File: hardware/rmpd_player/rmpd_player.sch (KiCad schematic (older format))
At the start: 37 parts

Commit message: spi stub
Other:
- moved on the sheet: C?, R?
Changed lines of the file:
@@
 L Device:R R?
 U 1 1 5C090195
-P 4400 1100
-F 0 "R?" H 4200 1150 50  0000 L CNN
-F 1 "10k" H 4200 1050 50  0000 L CNN
-F 2 "" V 4330 1100 50  0001 C CNN
-F 3 "~" H 4400 1100 50  0001 C CNN
-	1    4400 1100
-	1    0    0    -1
-$EndComp
-$Comp
-L Device:C C?
-U 1 1 5C0902B0
 P 4400 1500
-F 0 "C?" H 4550 1450 50  0000 C CNN
-F 1 "100n" H 4600 1550 50  0000 C CNN
-F 2 "" H 4438 1350 50  0001 C CNN
+F 0 "R?" H 4200 1550 50  0000 L CNN
+F 1 "10k" H 4200 1450 50  0000 L CNN
+F 2 "" V 4330 1500 50  0001 C CNN
 F 3 "~" H 4400 1500 50  0001 C CNN
 	1    4400 1500
-	-1   0    0    1
-$EndComp
-Text GLabel 4400 1700 3    50   Input ~ 0
+	1    0    0    -1
+$EndComp
+$Comp
+L Device:C C?
+U 1 1 5C0902B0
+P 4400 1900
+F 0 "C?" H 4550 1850 50  0000 C CNN
+F 1 "100n" H 4600 1950 50  0000 C CNN
+F 2 "" H 4438 1750 50  0001 C CNN
+F 3 "~" H 4400 1900 50  0001 C CNN
+	1    4400 1900
+	-1   0    0    1
+$EndComp
+Text GLabel 4400 2100 3    50   Input ~ 0
 GND
-Text GLabel 4400 900  1    50   Input ~ 0
+Text GLabel 4400 1300 1    50   Input ~ 0
 VDD
 Wire Wire Line
-	4400 900  4400 950
-Wire Wire Line
-	4400 1700 4400 1650
-Wire Wire Line
-	4400 1250 4400 1300
-Wire Wire Line
-	4400 1300 4650 1300
-Wire Wire Line
-	4650 1300 4650 1700
-Wire Wire Line
-	4650 1700 5050 1700
-Connection ~ 4400 1300
-Wire Wire Line
 	4400 1300 4400 1350
+Wire Wire Line
+	4400 2100 4400 2050
+Wire Wire Line
+	4400 1650 4400 1700
+Connection ~ 4400 1700
+Wire Wire Line
+	4400 1700 4400 1750
 Wire Wire Line
 	6900 2650 7250 2650
@@
 Wire Wire Line
 	6950 2350 6900 2350
-Text GLabel 2550 5750 0    50   Input ~ 0
+Text GLabel 2600 5750 0    50   Input ~ 0
 VDDA
-Text GLabel 3100 5750 2    50   Input ~ 0
+Text GLabel 3050 5750 2    50   Input ~ 0
 VDD
 $Comp
@@
 $EndComp
 Wire Wire Line
-	2550 5750 2700 5750
+	2600 5750 2700 5750
 Wire Wire Line
 	2950 5800 2950 5750
 Connection ~ 2950 5750
 Wire Wire Line
-	2950 5750 3100 5750
+	2950 5750 3050 5750
 Wire Wire Line
 	2700 5800 2700 5750
@@
 Wire Wire Line
 	2700 5750 2950 5750
-$Comp
-L power:GND #PWR?
-U 1 1 5C092AF6
-P 2950 6200
-F 0 "#PWR?" H 2950 5950 50  0001 C CNN
-F 1 "GND" H 2955 6027 50  0000 C CNN
-F 2 "" H 2950 6200 50  0001 C CNN
-F 3 "" H 2950 6200 50  0001 C CNN
-	1    2950 6200
-	1    0    0    -1
-$EndComp
-$Comp
-L power:GNDA #PWR?
-U 1 1 5C092B4B
-P 2700 6200
-F 0 "#PWR?" H 2700 5950 50  0001 C CNN
-F 1 "GNDA" H 2705 6027 50  0000 C CNN
-F 2 "" H 2700 6200 50  0001 C CNN
-F 3 "" H 2700 6200 50  0001 C CNN
-	1    2700 6200
-	1    0    0    -1
-$EndComp
-Wire Wire Line
-	2950 6100 2950 6200
-Wire Wire Line
-	2700 6100 2700 6200
+Wire Wire Line
+	2950 6100 2950 6150
+Wire Wire Line
+	2700 6100 2700 6150
+Wire Wire Line
+	4400 1700 5050 1700
+Text GLabel 2950 6150 3    50   Input ~ 0
+GND
+Text GLabel 2700 6150 3    50   Input ~ 0
+GNDA
 $EndSCHEMATC

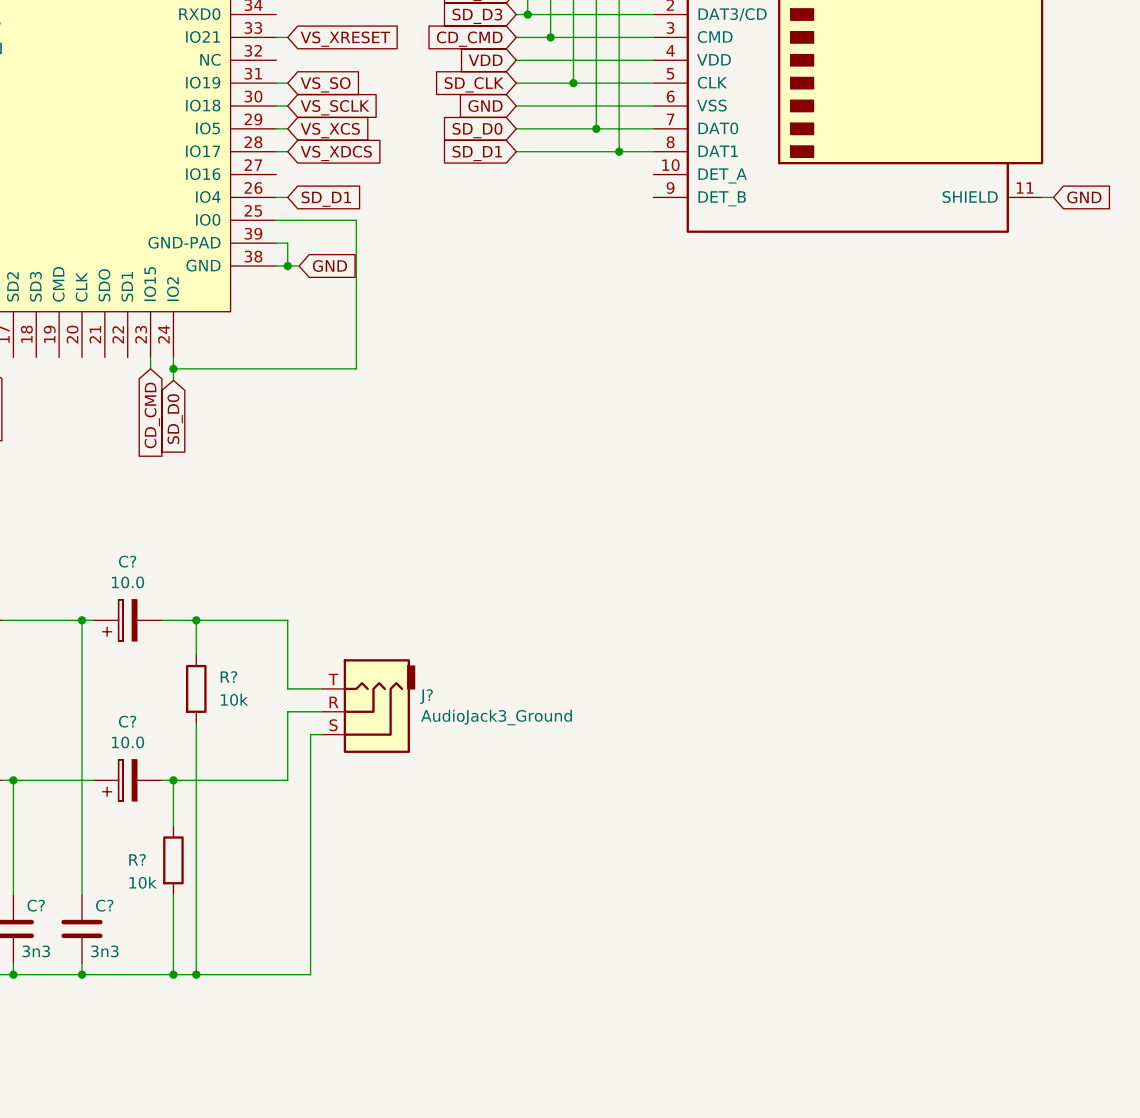
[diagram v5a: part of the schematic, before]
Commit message: vs1011 mute circuit
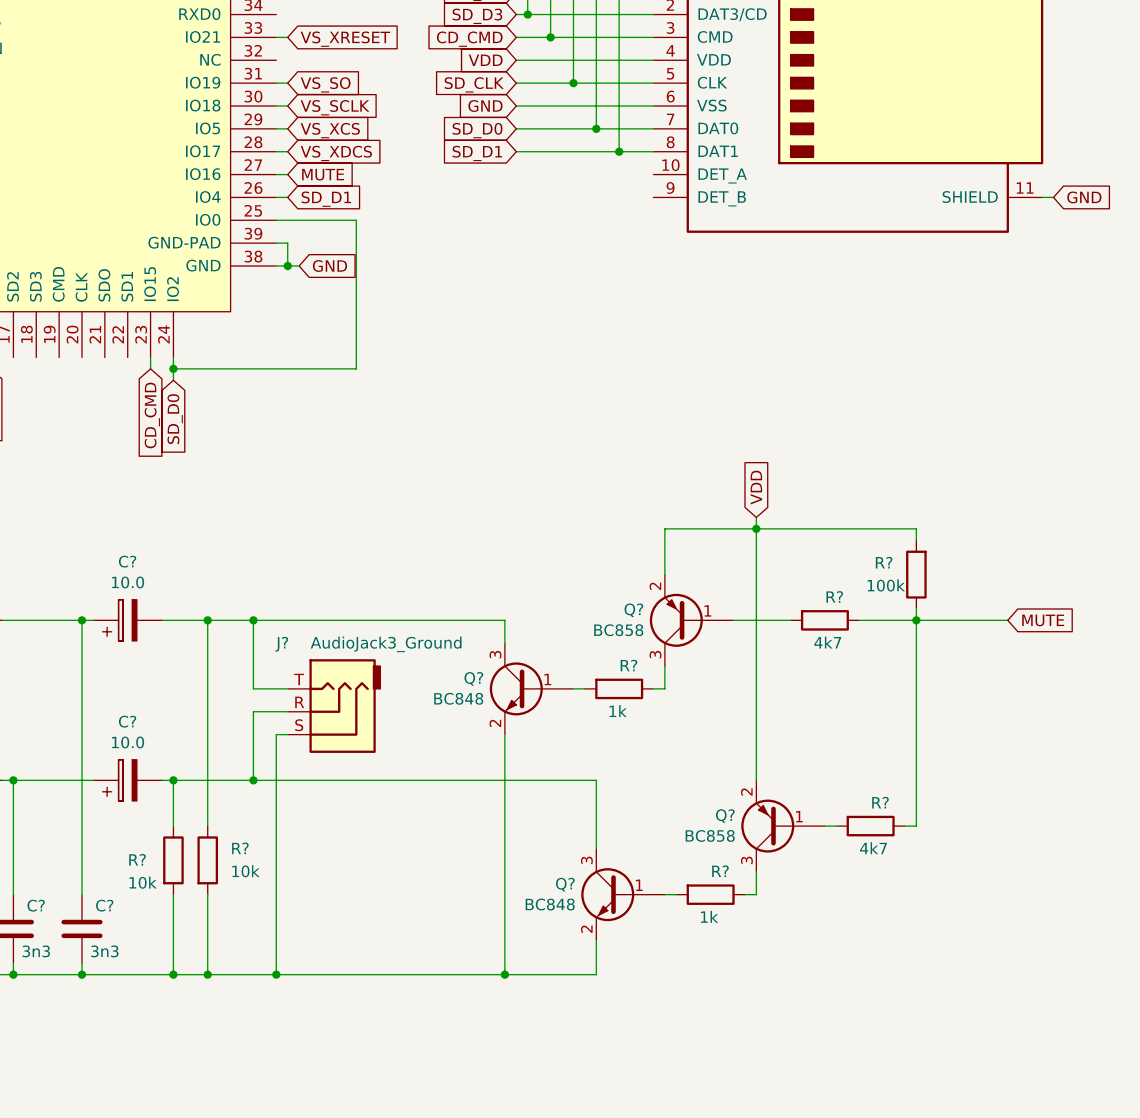
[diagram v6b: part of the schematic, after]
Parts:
- added Q? (x2): BC848, Package_TO_SOT_SMD:SOT-23, symbol Transistor_BJT:BC848
- added Q? (x2): BC858, Package_TO_SOT_SMD:SOT-23, symbol Transistor_BJT:BC858
- added R? (x2): 1k, symbol Device:R
- added R?: 100k, symbol Device:R
- added R? (x2): 4k7, symbol Device:R
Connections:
- net GND: now also Q?.2 (E), Q?.2 (E)
- net VDD: now also Q?.2 (E), Q?.2 (E), R?.2
- net MUTE: now reaches U?.27 (IO16)
- net MUTE: now also R?.1, R?.1, R?.1
- net at C?.2, J?.T, R?.1: now also Q?.3 (C)
- net at C?.2, J?.R, R?.1: now also Q?.3 (C)
- new net: Q?.1 (B), R?.2 (x4)
- new net: Q?.3 (C), R?.1 (x2)
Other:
- moved on the sheet: J?, R?
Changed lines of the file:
@@
 L Device:R R?
 U 1 1 5C29D83E
-P 6550 4700
-F 0 "R?" H 6650 4750 50  0000 L CNN
-F 1 "10k" H 6650 4650 50  0000 L CNN
-F 2 "" V 6480 4700 50  0001 C CNN
-F 3 "~" H 6550 4700 50  0001 C CNN
-	1    6550 4700
+P 6600 5450
+F 0 "R?" H 6700 5500 50  0000 L CNN
+F 1 "10k" H 6700 5400 50  0000 L CNN
+F 2 "" V 6530 5450 50  0001 C CNN
+F 3 "~" H 6600 5450 50  0001 C CNN
+	1    6600 5450
 	1    0    0    -1
 $EndComp
@@
 Connection ~ 6050 5950
 Wire Wire Line
-	6400 4400 6550 4400
-Wire Wire Line
-	6550 4400 6550 4550
-Wire Wire Line
-	6550 4850 6550 5950
-Wire Wire Line
-	6550 5950 6450 5950
+	6400 4400 6600 4400
+Wire Wire Line
+	6600 4400 6600 5300
+Wire Wire Line
+	6600 5600 6600 5950
+Wire Wire Line
+	6600 5950 6450 5950
 Connection ~ 6450 5950
 $Comp
 L Connector:AudioJack3_Ground J?
 U 1 1 5C2C1C35
-P 7300 4800
-F 0 "J?" H 7067 4729 50  0000 R CNN
-F 1 "AudioJack3_Ground" H 7067 4820 50  0000 R CNN
-F 2 "" H 7300 4800 50  0001 C CNN
-F 3 "~" H 7300 4800 50  0001 C CNN
-	1    7300 4800
+P 7150 4800
+F 0 "J?" H 7400 4500 50  0000 R CNN
+F 1 "AudioJack3_Ground" H 7250 4500 50  0000 R CNN
+F 2 "" H 7150 4800 50  0001 C CNN
+F 3 "~" H 7150 4800 50  0001 C CNN
+	1    7150 4800
 	-1   0    0    1
 $EndComp
 Wire Wire Line
-	6550 4400 6950 4400
-Wire Wire Line
-	6950 4400 6950 4700
-Wire Wire Line
-	6950 4700 7100 4700
-Connection ~ 6550 4400
-Wire Wire Line
-	6450 5100 6950 5100
-Wire Wire Line
-	6950 5100 6950 4800
-Wire Wire Line
-	6950 4800 7100 4800
+	6600 4400 6800 4400
+Wire Wire Line
+	6800 4400 6800 4700
+Wire Wire Line
+	6800 4700 6950 4700
+Connection ~ 6600 4400
+Wire Wire Line
+	6450 5100 6800 5100
+Wire Wire Line
+	6800 5100 6800 4800
+Wire Wire Line
+	6800 4800 6950 4800
 Connection ~ 6450 5100
 Wire Wire Line
-	6550 5950 7050 5950
-Wire Wire Line
-	7050 5950 7050 4900
-Wire Wire Line
-	7050 4900 7100 4900
-Connection ~ 6550 5950
+	6600 5950 6900 5950
+Wire Wire Line
+	6900 5950 6900 4900
+Wire Wire Line
+	6900 4900 6950 4900
+Connection ~ 6600 5950
 $Comp
 L Device:R R?
@@
 Text GLabel 2700 6150 3    50   Input ~ 0
 GNDA
+$Comp
+L Transistor_BJT:BC848 Q?
+U 1 1 5C055DAE
+P 8000 4700
+F 0 "Q?" H 8190 4746 50  0000 L CNN
+F 1 "BC848" H 8190 4655 50  0000 L CNN
+F 2 "Package_TO_SOT_SMD:SOT-23" H 8200 4625 50  0001 L CIN
+F 3 "http://www.infineon.com/dgdl/Infineon-BC847SERIES_BC848SERIES_BC849SERIES_BC850SERIES-DS-v01_01-en.pdf?fileId=db3a304314dca389011541d4630a1657" H 8000 4700 50  0001 L CNN
+	1    8000 4700
+	-1   0    0    -1
+$EndComp
+$Comp
+L Transistor_BJT:BC848 Q?
+U 1 1 5C056099
+P 8400 5600
+F 0 "Q?" H 8590 5646 50  0000 L CNN
+F 1 "BC848" H 8590 5555 50  0000 L CNN
+F 2 "Package_TO_SOT_SMD:SOT-23" H 8600 5525 50  0001 L CIN
+F 3 "http://www.infineon.com/dgdl/Infineon-BC847SERIES_BC848SERIES_BC849SERIES_BC850SERIES-DS-v01_01-en.pdf?fileId=db3a304314dca389011541d4630a1657" H 8400 5600 50  0001 L CNN
+	1    8400 5600
+	-1   0    0    -1
+$EndComp
+Wire Wire Line
+	6800 4400 7900 4400
+Wire Wire Line
+	7900 4400 7900 4500
+Connection ~ 6800 4400
+Wire Wire Line
+	8300 5400 8300 5100
+Wire Wire Line
+	8300 5100 6800 5100
+Connection ~ 6800 5100
+Wire Wire Line
+	7900 5950 6900 5950
+Connection ~ 6900 5950
+Wire Wire Line
+	8300 5800 8300 5950
+Wire Wire Line
+	8300 5950 7900 5950
+Connection ~ 7900 5950
+Wire Wire Line
+	7900 4900 7900 5950
+$Comp
+L Device:R R?
+U 1 1 5C0BA812
+P 8400 4700
+F 0 "R?" V 8300 4700 50  0000 L CNN
+F 1 "1k" V 8500 4650 50  0000 L CNN
+F 2 "" V 8330 4700 50  0001 C CNN
+F 3 "~" H 8400 4700 50  0001 C CNN
+	1    8400 4700
+	0    1    1    0
+$EndComp
+$Comp
+L Device:R R?
+U 1 1 5C0BAA8F
+P 8800 5600
+F 0 "R?" V 8700 5600 50  0000 L CNN
+F 1 "1k" V 8900 5550 50  0000 L CNN
+F 2 "" V 8730 5600 50  0001 C CNN
+F 3 "~" H 8800 5600 50  0001 C CNN
+	1    8800 5600
+	0    1    1    0
+$EndComp
+$Comp
+L Transistor_BJT:BC858 Q?
+U 1 1 5C0BAC2A
+P 8700 4400
+F 0 "Q?" H 8890 4354 50  0000 L CNN
+F 1 "BC858" H 8890 4445 50  0000 L CNN
+F 2 "Package_TO_SOT_SMD:SOT-23" H 8900 4325 50  0001 L CIN
+F 3 "http://www.fairchildsemi.com/ds/BC/BC856.pdf" H 8700 4400 50  0001 L CNN
+	1    8700 4400
+	-1   0    0    1
+$EndComp
+$Comp
+L Transistor_BJT:BC858 Q?
+U 1 1 5C0BADDA
+P 9100 5300
+F 0 "Q?" H 9290 5254 50  0000 L CNN
+F 1 "BC858" H 9290 5345 50  0000 L CNN
+F 2 "Package_TO_SOT_SMD:SOT-23" H 9300 5225 50  0001 L CIN
+F 3 "http://www.fairchildsemi.com/ds/BC/BC856.pdf" H 9100 5300 50  0001 L CNN
+	1    9100 5300
+	-1   0    0    1
+$EndComp
+$Comp
+L Device:R R?
+U 1 1 5C0BB062
+P 9700 4200
+F 0 "R?" H 9800 4150 50  0000 L CNN
+F 1 "100k" H 9750 4250 50  0000 L CNN
+F 2 "" V 9630 4200 50  0001 C CNN
+F 3 "~" H 9700 4200 50  0001 C CNN
+	1    9700 4200
+	-1   0    0    1
+$EndComp
+$Comp
+L Device:R R?
+U 1 1 5C0BB3CA
+P 9300 4400
+F 0 "R?" V 9200 4400 50  0000 L CNN
+F 1 "4k7" V 9400 4350 50  0000 L CNN
+F 2 "" V 9230 4400 50  0001 C CNN
+F 3 "~" H 9300 4400 50  0001 C CNN
+	1    9300 4400
+	0    1    1    0
+$EndComp
+$Comp
+L Device:R R?
+U 1 1 5C0BB458
+P 9500 5300
+F 0 "R?" V 9400 5300 50  0000 L CNN
+F 1 "4k7" V 9600 5250 50  0000 L CNN
+F 2 "" V 9430 5300 50  0001 C CNN
+F 3 "~" H 9500 5300 50  0001 C CNN
+	1    9500 5300
+	0    1    1    0
+$EndComp
+Wire Wire Line
+	8900 4400 9150 4400
+Wire Wire Line
+	9450 4400 9700 4400
+Wire Wire Line
+	9700 4400 9700 5300
+Wire Wire Line
+	9700 5300 9650 5300
+Wire Wire Line
+	9700 4350 9700 4400
+Connection ~ 9700 4400
+Wire Wire Line
+	8550 4700 8600 4700
+Wire Wire Line
+	8600 4700 8600 4600
+Wire Wire Line
+	8950 5600 9000 5600
+Wire Wire Line
+	9000 5600 9000 5500
+Wire Wire Line
+	8600 5600 8650 5600
+Wire Wire Line
+	8200 4700 8250 4700
+Wire Wire Line
+	8600 4200 8600 4000
+Wire Wire Line
+	8600 4000 9000 4000
+Wire Wire Line
+	9700 4000 9700 4050
+Wire Wire Line
+	9000 5100 9000 4000
+Connection ~ 9000 4000
+Wire Wire Line
+	9000 4000 9700 4000
+Text GLabel 9000 3950 1    50   Input ~ 0
+VDD
+Wire Wire Line
+	9000 4000 9000 3950
+Wire Wire Line
+	9350 5300 9300 5300
+Text GLabel 10100 4400 2    50   Input ~ 0
+MUTE
+Wire Wire Line
+	10100 4400 9700 4400
+Text GLabel 6950 2450 2    50   Input ~ 0
+MUTE
+Wire Wire Line
+	6900 2450 6950 2450
 $EndSCHEMATC

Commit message: lm1117 schematic
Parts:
- added C? (x2): 100n, symbol Device:C
- added C? (x2): 10.0, symbol Device:CP
- added D?: 5.1V, symbol Device:D_Zener
- added F?: Fuse, symbol Device:Fuse
- added J?: Barrel_Jack, symbol Connector:Barrel_Jack
- added U?: LM1117-3.3, symbol Regulator_Linear:LM1117-3.3
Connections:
- net GND: now also C?.2, C?.2, C?.2, C?.2, D?.2 (A), J?.2, U?.1 (GND)
- net VDD: now also C?.1, C?.1, C?.1, U?.2 (VO)
- new net: C?.1, D?.1 (K), F?.2, U?.3 (VI)
- new net: F?.1, J?.1
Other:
- note removed: "Connect GND and GNDA close to VS1011"
- moved on the sheet: C?
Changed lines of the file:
@@
 Wire Wire Line
 	1700 5850 1700 6050
-Text Notes 800  6400 0    50   ~ 0
-Connect GND and GNDA close to VS1011
 $Comp
 L Device:R R?
@@
 Text GLabel 2600 5750 0    50   Input ~ 0
 VDDA
-Text GLabel 3050 5750 2    50   Input ~ 0
+Text GLabel 3550 5750 2    50   Input ~ 0
 VDD
 $Comp
@@
 L Device:C C?
 U 1 1 5C06DC75
-P 2950 5950
-F 0 "C?" H 3050 6050 50  0000 C CNN
-F 1 "100n" H 3050 5850 50  0000 C CNN
-F 2 "" H 2988 5800 50  0001 C CNN
-F 3 "~" H 2950 5950 50  0001 C CNN
-	1    2950 5950
+P 3450 5950
+F 0 "C?" H 3550 6050 50  0000 C CNN
+F 1 "100n" H 3550 5850 50  0000 C CNN
+F 2 "" H 3488 5800 50  0001 C CNN
+F 3 "~" H 3450 5950 50  0001 C CNN
+	1    3450 5950
 	1    0    0    -1
 $EndComp
@@
 	2600 5750 2700 5750
 Wire Wire Line
-	2950 5800 2950 5750
-Connection ~ 2950 5750
-Wire Wire Line
-	2950 5750 3050 5750
+	3450 5800 3450 5750
+Connection ~ 3450 5750
+Wire Wire Line
+	3450 5750 3550 5750
 Wire Wire Line
 	2700 5800 2700 5750
@@
 	2700 5750 2950 5750
 Wire Wire Line
-	2950 6100 2950 6150
+	3450 6100 3450 6150
 Wire Wire Line
 	2700 6100 2700 6150
 Wire Wire Line
 	4400 1700 5050 1700
-Text GLabel 2950 6150 3    50   Input ~ 0
+Text GLabel 3450 6150 3    50   Input ~ 0
 GND
 Text GLabel 2700 6150 3    50   Input ~ 0
@@
 Wire Wire Line
 	6900 2450 6950 2450
+$Comp
+L Device:C C?
+U 1 1 5C08CC4A
+P 2950 5950
+F 0 "C?" H 3050 6050 50  0000 C CNN
+F 1 "100n" H 3050 5850 50  0000 C CNN
+F 2 "" H 2988 5800 50  0001 C CNN
+F 3 "~" H 2950 5950 50  0001 C CNN
+	1    2950 5950
+	1    0    0    -1
+$EndComp
+$Comp
+L Device:C C?
+U 1 1 5C08CCC0
+P 3200 5950
+F 0 "C?" H 3300 6050 50  0000 C CNN
+F 1 "100n" H 3300 5850 50  0000 C CNN
+F 2 "" H 3238 5800 50  0001 C CNN
+F 3 "~" H 3200 5950 50  0001 C CNN
+	1    3200 5950
+	1    0    0    -1
+$EndComp
+Wire Wire Line
+	2950 5800 2950 5750
+Connection ~ 2950 5750
+Wire Wire Line
+	2950 5750 3200 5750
+Wire Wire Line
+	3200 5800 3200 5750
+Connection ~ 3200 5750
+Wire Wire Line
+	3200 5750 3450 5750
+Text GLabel 2950 6150 3    50   Input ~ 0
+GNDA
+Text GLabel 3200 6150 3    50   Input ~ 0
+GND
+Wire Wire Line
+	2950 6100 2950 6150
+Wire Wire Line
+	3200 6100 3200 6150
+$Comp
+L Regulator_Linear:LM1117-3.3 U?
+U 1 1 5C0BDAEC
+P 2450 1750
+F 0 "U?" H 2450 1992 50  0000 C CNN
+F 1 "LM1117-3.3" H 2450 1901 50  0000 C CNN
+F 2 "" H 2450 1750 50  0001 C CNN
+F 3 "http://www.ti.com/lit/ds/symlink/lm1117.pdf" H 2450 1750 50  0001 C CNN
+	1    2450 1750
+	1    0    0    -1
+$EndComp
+$Comp
+L Device:CP C?
+U 1 1 5C0BE156
+P 2050 2000
+F 0 "C?" H 1850 2050 50  0000 C CNN
+F 1 "10.0" H 1850 1950 50  0000 C CNN
+F 2 "" H 2088 1850 50  0001 C CNN
+F 3 "~" H 2050 2000 50  0001 C CNN
+	1    2050 2000
+	1    0    0    -1
+$EndComp
+$Comp
+L Device:CP C?
+U 1 1 5C0BE7B4
+P 2850 2000
+F 0 "C?" H 3050 2050 50  0000 C CNN
+F 1 "10.0" H 3050 1950 50  0000 C CNN
+F 2 "" H 2888 1850 50  0001 C CNN
+F 3 "~" H 2850 2000 50  0001 C CNN
+	1    2850 2000
+	1    0    0    -1
+$EndComp
+Wire Wire Line
+	2150 1750 2050 1750
+Wire Wire Line
+	2050 1750 2050 1850
+Wire Wire Line
+	2050 2150 2050 2200
+Wire Wire Line
+	2050 2200 2450 2200
+Wire Wire Line
+	2850 2200 2850 2150
+Wire Wire Line
+	2450 2050 2450 2200
+Connection ~ 2450 2200
+Wire Wire Line
+	2450 2200 2850 2200
+Wire Wire Line
+	2750 1750 2850 1750
+Wire Wire Line
+	2850 1750 2850 1850
+Text GLabel 2450 2250 3    50   Input ~ 0
+GND
+Wire Wire Line
+	2450 2250 2450 2200
+Text GLabel 3000 1750 2    50   Input ~ 0
+VDD
+Text GLabel 3000 1650 2    50   Input ~ 0
+VDDA
+Wire Wire Line
+	3000 1650 2850 1650
+Wire Wire Line
+	2850 1650 2850 1750
+Connection ~ 2850 1750
+Wire Wire Line
+	2850 1750 3000 1750
+$Comp
+L Connector:Barrel_Jack J?
+U 1 1 5C11E4C3
+P 950 1850
+F 0 "J?" H 1005 2175 50  0000 C CNN
+F 1 "Barrel_Jack" H 1005 2084 50  0000 C CNN
+F 2 "" H 1000 1810 50  0001 C CNN
+F 3 "~" H 1000 1810 50  0001 C CNN
+	1    950  1850
+	1    0    0    -1
+$EndComp
+Connection ~ 2050 1750
+Wire Wire Line
+	1250 1950 1300 1950
+Wire Wire Line
+	1300 1950 1300 2200
+Connection ~ 2050 2200
+Wire Wire Line
+	1250 1750 1350 1750
+Wire Wire Line
+	1300 2200 1700 2200
+$Comp
+L Device:Fuse F?
+U 1 1 5C16C081
+P 1500 1750
+F 0 "F?" V 1697 1750 50  0000 C CNN
+F 1 "Fuse" V 1606 1750 50  0000 C CNN
+F 2 "" V 1430 1750 50  0001 C CNN
+F 3 "~" H 1500 1750 50  0001 C CNN
+	1    1500 1750
+	0    -1   -1   0
+$EndComp
+Wire Wire Line
+	1650 1750 1700 1750
+$Comp
+L Device:D_Zener D?
+U 1 1 5C19A59E
+P 1700 2000
+F 0 "D?" V 1650 1800 50  0000 L CNN
+F 1 "5.1V" V 1750 1750 50  0000 L CNN
+F 2 "" H 1700 2000 50  0001 C CNN
+F 3 "~" H 1700 2000 50  0001 C CNN
+	1    1700 2000
+	0    1    1    0
+$EndComp
+Wire Wire Line
+	1700 1750 1700 1850
+Connection ~ 1700 1750
+Wire Wire Line
+	1700 1750 2050 1750
+Wire Wire Line
+	1700 2150 1700 2200
+Connection ~ 1700 2200
+Wire Wire Line
+	1700 2200 2050 2200
 $EndSCHEMATC

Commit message: scheduler added
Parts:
- R? (x2): value 1k -> 10k
- R? (x2): value 4k7 -> 10k
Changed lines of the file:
@@
 P 8400 4700
 F 0 "R?" V 8300 4700 50  0000 L CNN
-F 1 "1k" V 8500 4650 50  0000 L CNN
+F 1 "10k" V 8500 4650 50  0000 L CNN
 F 2 "" V 8330 4700 50  0001 C CNN
 F 3 "~" H 8400 4700 50  0001 C CNN
@@
 P 8800 5600
 F 0 "R?" V 8700 5600 50  0000 L CNN
-F 1 "1k" V 8900 5550 50  0000 L CNN
+F 1 "10k" V 8900 5550 50  0000 L CNN
 F 2 "" V 8730 5600 50  0001 C CNN
 F 3 "~" H 8800 5600 50  0001 C CNN
@@
 P 9300 4400
 F 0 "R?" V 9200 4400 50  0000 L CNN
-F 1 "4k7" V 9400 4350 50  0000 L CNN
+F 1 "10k" V 9400 4350 50  0000 L CNN
 F 2 "" V 9230 4400 50  0001 C CNN
 F 3 "~" H 9300 4400 50  0001 C CNN
@@
 P 9500 5300
 F 0 "R?" V 9400 5300 50  0000 L CNN
-F 1 "4k7" V 9600 5250 50  0000 L CNN
+F 1 "10k" V 9600 5250 50  0000 L CNN
 F 2 "" V 9430 5300 50  0001 C CNN
 F 3 "~" H 9500 5300 50  0001 C CNN
